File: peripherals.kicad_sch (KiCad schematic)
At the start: 18 parts, among them IC5 ${ALTIUM_VALUE}, IC6 ${ALTIUM_VALUE}, IC7 ${ALTIUM_VALUE}, J7 *

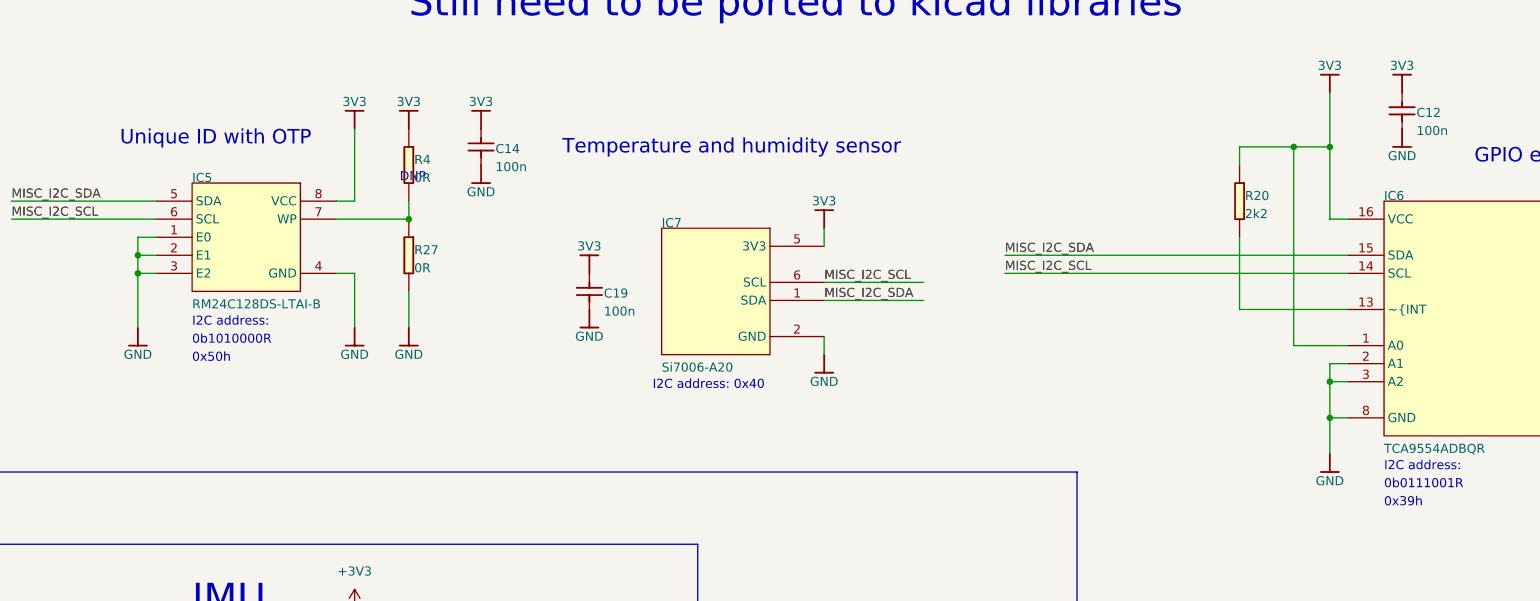
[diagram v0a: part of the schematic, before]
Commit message: Added loclib, updated README and added pdf schematic
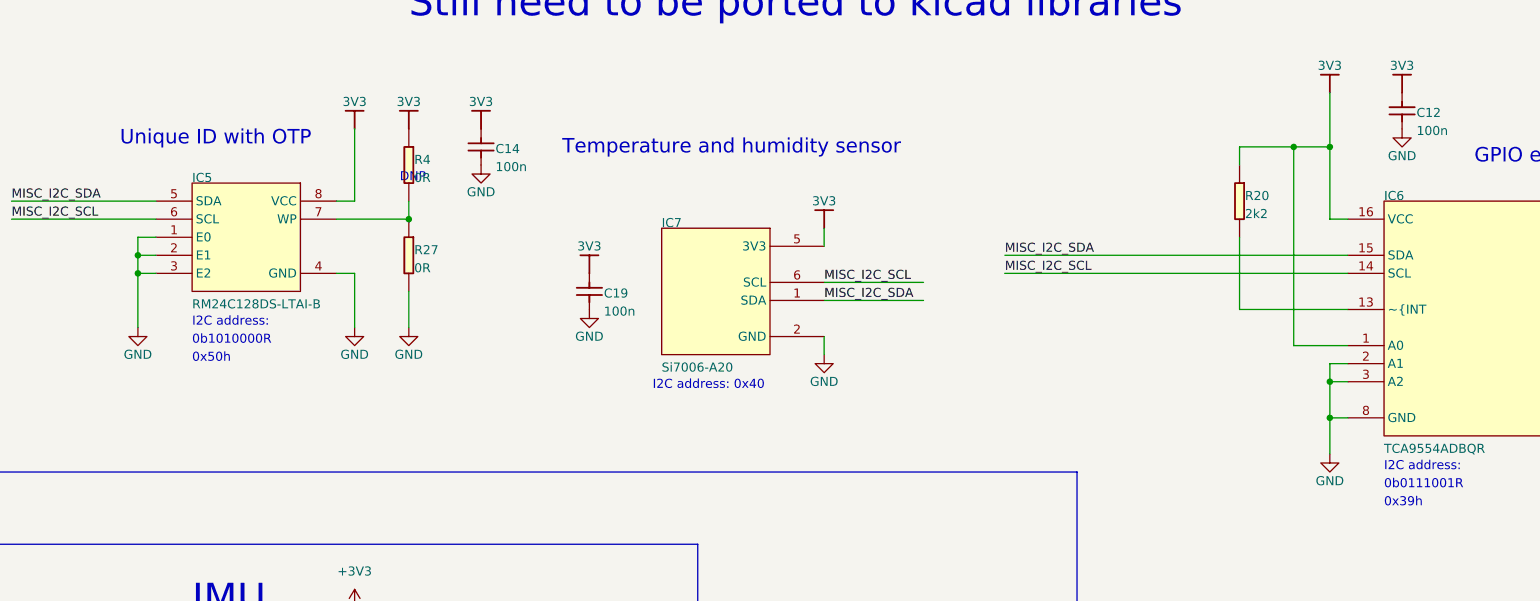
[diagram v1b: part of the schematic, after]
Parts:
- C12, C14: footprint 0603 -> antmicro-jetson-agx-csi-adapter-footprints:0603; symbol Peripherals-altium-import:1_C -> antmicro-jetson-agx-csi-adapter:1_C
- C19: footprint 0402 -> antmicro-jetson-agx-csi-adapter-footprints:0402; symbol Peripherals-altium-import:1_C -> antmicro-jetson-agx-csi-adapter:1_C
- C?: footprint antmicro-footprints:0402-cap -> antmicro-jetson-agx-csi-adapter-footprints:0402-cap; symbol antmicroCapacitors0402:C_10n_0402 -> antmicro-jetson-agx-csi-adapter:C_10n_0402
- C? (x3): footprint antmicro-footprints:0402-cap -> antmicro-jetson-agx-csi-adapter-footprints:0402-cap; symbol antmicroCapacitors0402:C_100n_0402 -> antmicro-jetson-agx-csi-adapter:C_100n_0402
- IC5: footprint TSSOP-8 -> antmicro-jetson-agx-csi-adapter-footprints:TSSOP-8; symbol Peripherals-altium-import:0_RM24C128DS -> antmicro-jetson-agx-csi-adapter:0_RM24C128DS
- IC6: footprint DBQ0016A -> antmicro-jetson-agx-csi-adapter-footprints:DBQ0016A; symbol Peripherals-altium-import:0_TCA9554A -> antmicro-jetson-agx-csi-adapter:0_TCA9554A
- IC7: footprint Si7006-A20 -> antmicro-jetson-agx-csi-adapter-footprints:Si7006-A20; symbol Peripherals-altium-import:0_Si7006 -> antmicro-jetson-agx-csi-adapter:0_Si7006
- J7: footprint HEADER_1X4_male 2.54mm angle -> antmicro-jetson-agx-csi-adapter-footprints:HEADER_1X4_male 2.54mm angle; symbol Peripherals-altium-import:0_HEADER_1X4_male_angle -> antmicro-jetson-agx-csi-adapter:0_HEADER_1X4_male_angle
- R20, R27, R4: footprint 0603 -> antmicro-jetson-agx-csi-adapter-footprints:0603; symbol Peripherals-altium-import:1_R -> antmicro-jetson-agx-csi-adapter:1_R
- R? (x2): footprint antmicro-footprints:0402-res -> antmicro-jetson-agx-csi-adapter-footprints:0402-res; symbol antmicroResistors0402:R_10k_0402 -> antmicro-jetson-agx-csi-adapter:R_10k_0402
- R?: footprint antmicro-footprints:0402-res -> antmicro-jetson-agx-csi-adapter-footprints:0402-res; symbol antmicroResistors0402:R_0R_0402 -> antmicro-jetson-agx-csi-adapter:R_0R_0402
- U?: footprint antmicro-footprints:LGA-28_5.2x3.8mm_BNO0055 -> antmicro-jetson-agx-csi-adapter-footprints:LGA-28_5.2x3.8mm_BNO0055; symbol antmicroMotionSensorsIMUsInertialMeasurementUnits:BNO055 -> antmicro-jetson-agx-csi-adapter:BNO055
